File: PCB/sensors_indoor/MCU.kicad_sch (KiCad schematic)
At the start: 14 parts, among them J2 STDC14, SW1 TL3305, U2 STM32WBA5MMG, U3 FM24CL16B

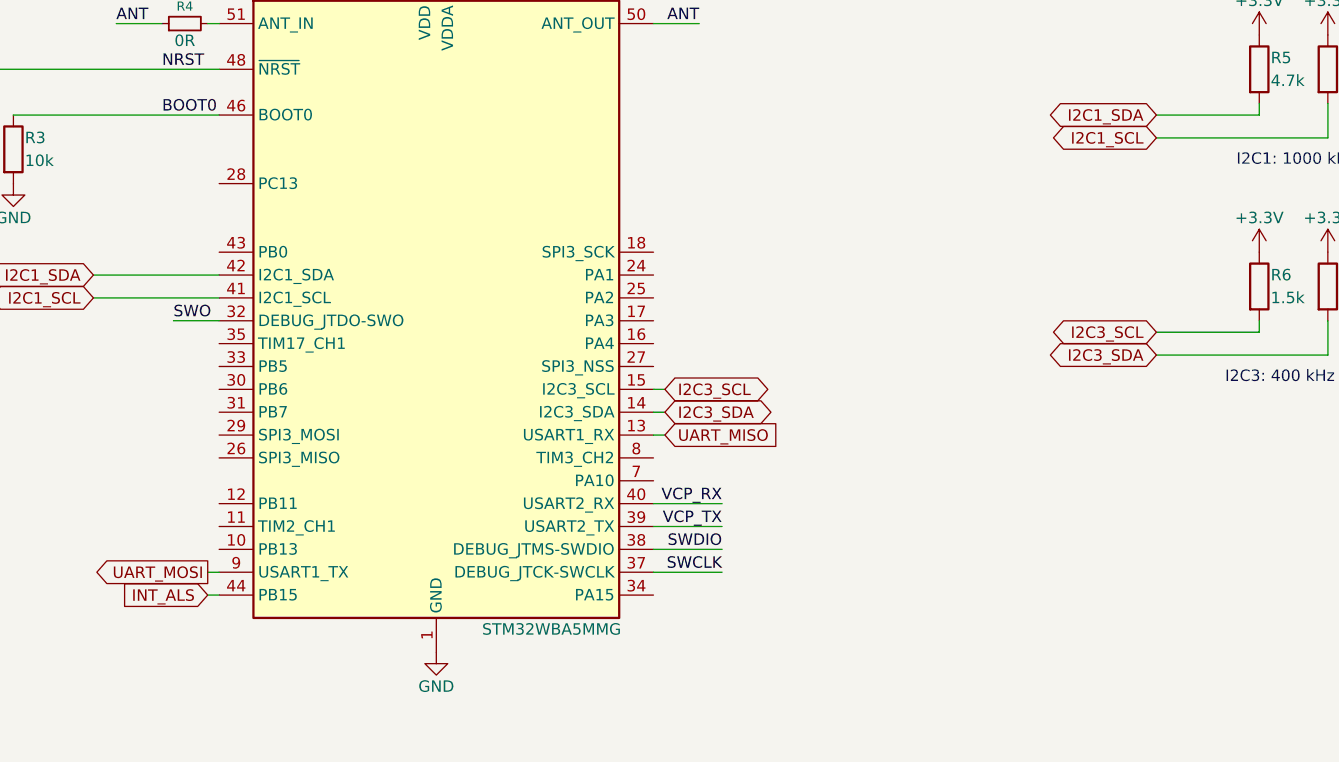
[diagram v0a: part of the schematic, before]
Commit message: Added LEDs
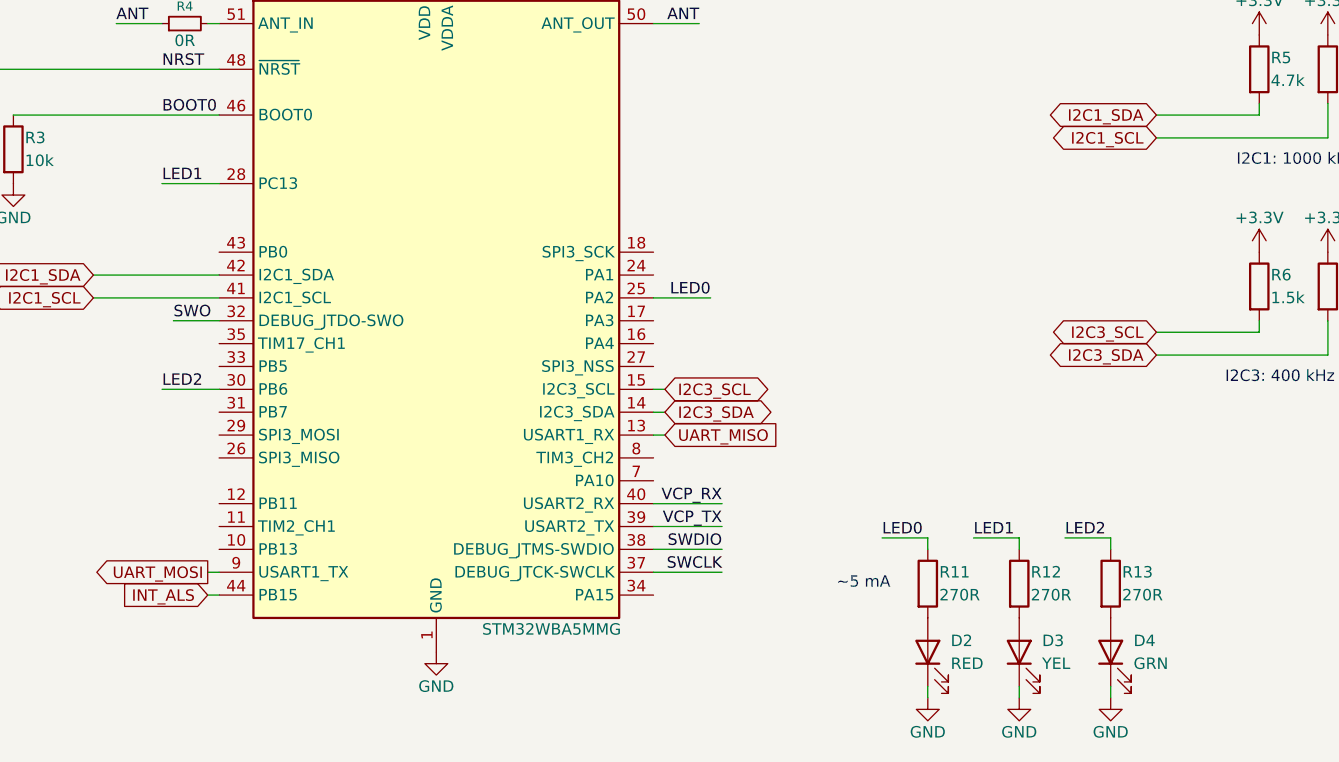
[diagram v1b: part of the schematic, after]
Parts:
- added D2: RED, LED_SMD:LED_0805_2012Metric, symbol Device:LED
- added D3: YEL, LED_SMD:LED_0805_2012Metric, symbol Device:LED
- added D4: GRN, LED_SMD:LED_0805_2012Metric, symbol Device:LED
- added R11, R12, R13: 270R, Resistor_SMD:R_0603_1608Metric, symbol Device:R
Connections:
- net GND: now also D2.1 (K), D3.1 (K), D4.1 (K)
- net LED0: now reaches U2.25 (PA2)
- net LED0: now also R11.1
- net LED1: now reaches U2.28 (PC13)
- net LED1: now also R12.1
- net LED2: now reaches U2.30 (PB6)
- net LED2: now also R13.1
- new net: D4.2 (A), R13.2
- new net: D3.2 (A), R12.2
- new net: D2.2 (A), R11.2
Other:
- note added: "~5 mA"

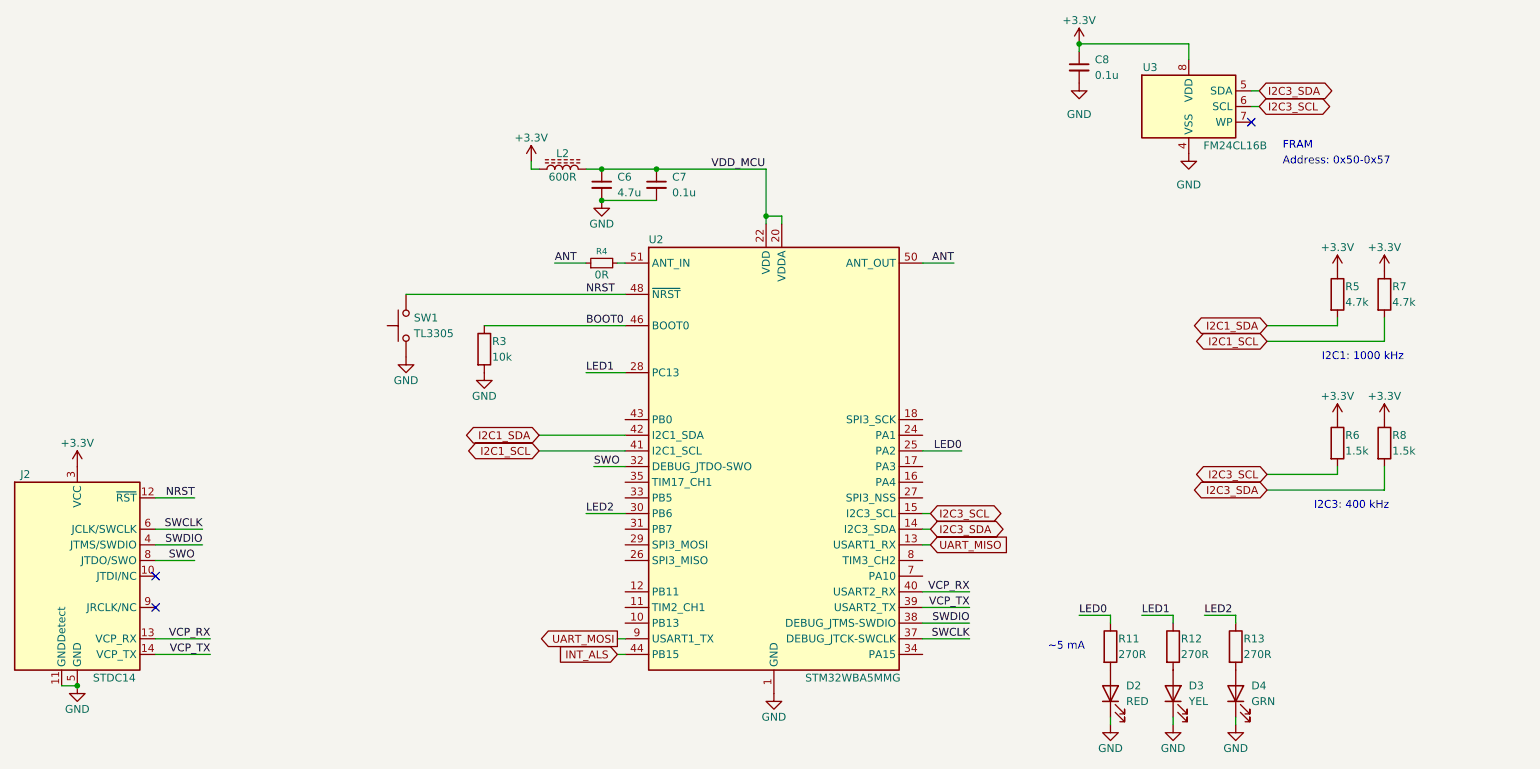
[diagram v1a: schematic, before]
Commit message: Rotated USB-C to exit at bottom, added debug pins for I2C
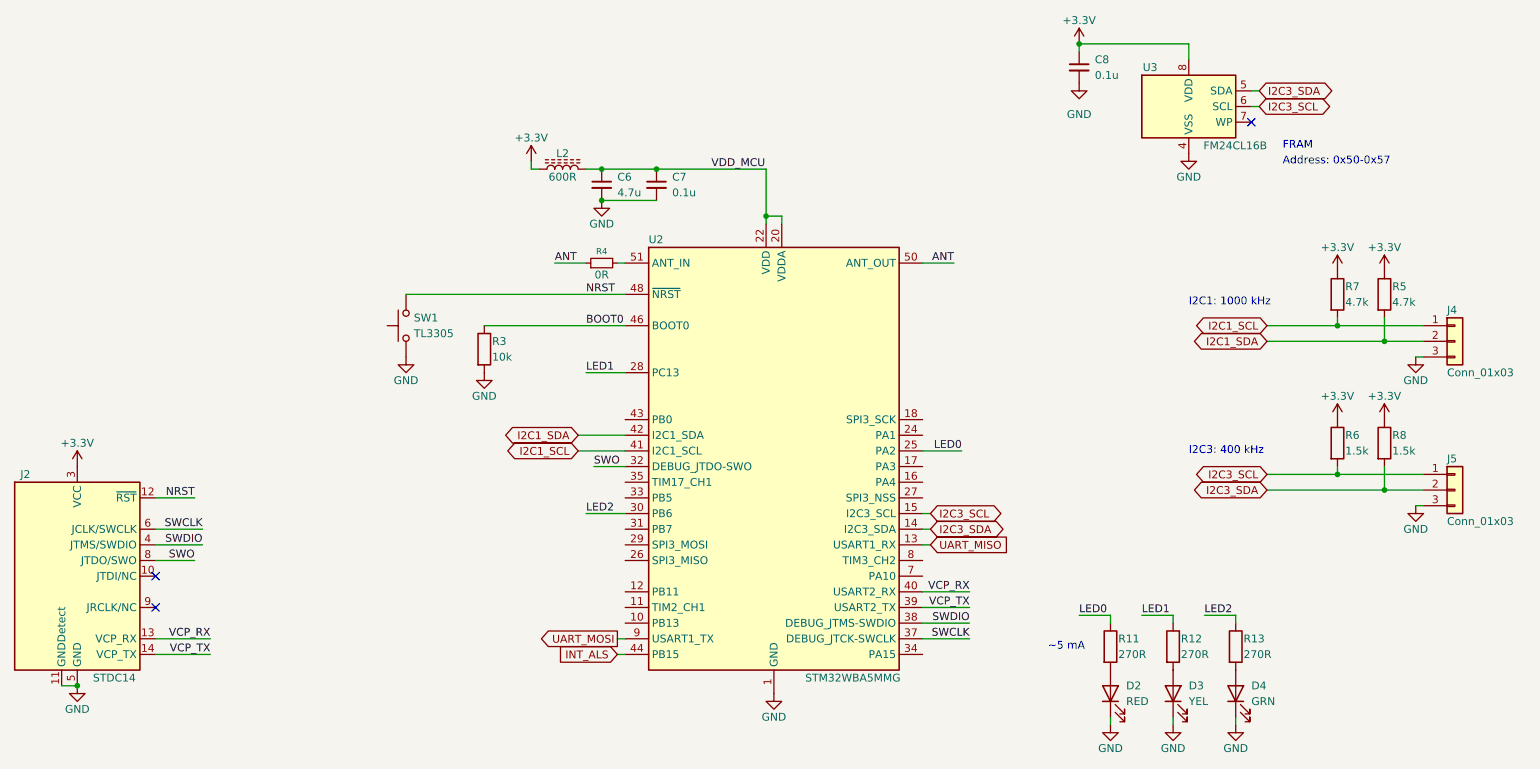
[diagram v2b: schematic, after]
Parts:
- added J4, J5: Conn_01x03, Connector_PinHeader_2.54mm:PinHeader_1x03_P2.54mm_Vertical, symbol Connector_Generic:Conn_01x03
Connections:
- net GND: now also J4.3 (Pin_3), J5.3 (Pin_3)
- net I2C1_SCL: now also J4.1 (Pin_1)
- net I2C1_SDA: now also J4.2 (Pin_2)
- net I2C3_SCL: now also J5.1 (Pin_1)
- net I2C3_SDA: now also J5.2 (Pin_2)
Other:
- moved on the sheet: R5, R7
